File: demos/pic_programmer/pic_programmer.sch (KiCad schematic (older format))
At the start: 50 parts, among them J1 DB9-FEMAL, P1 CONN_2, Q1 BC237, Q2 BC307, Q3 BC307, U2 74HC125, U3 7805, U4 LT1373

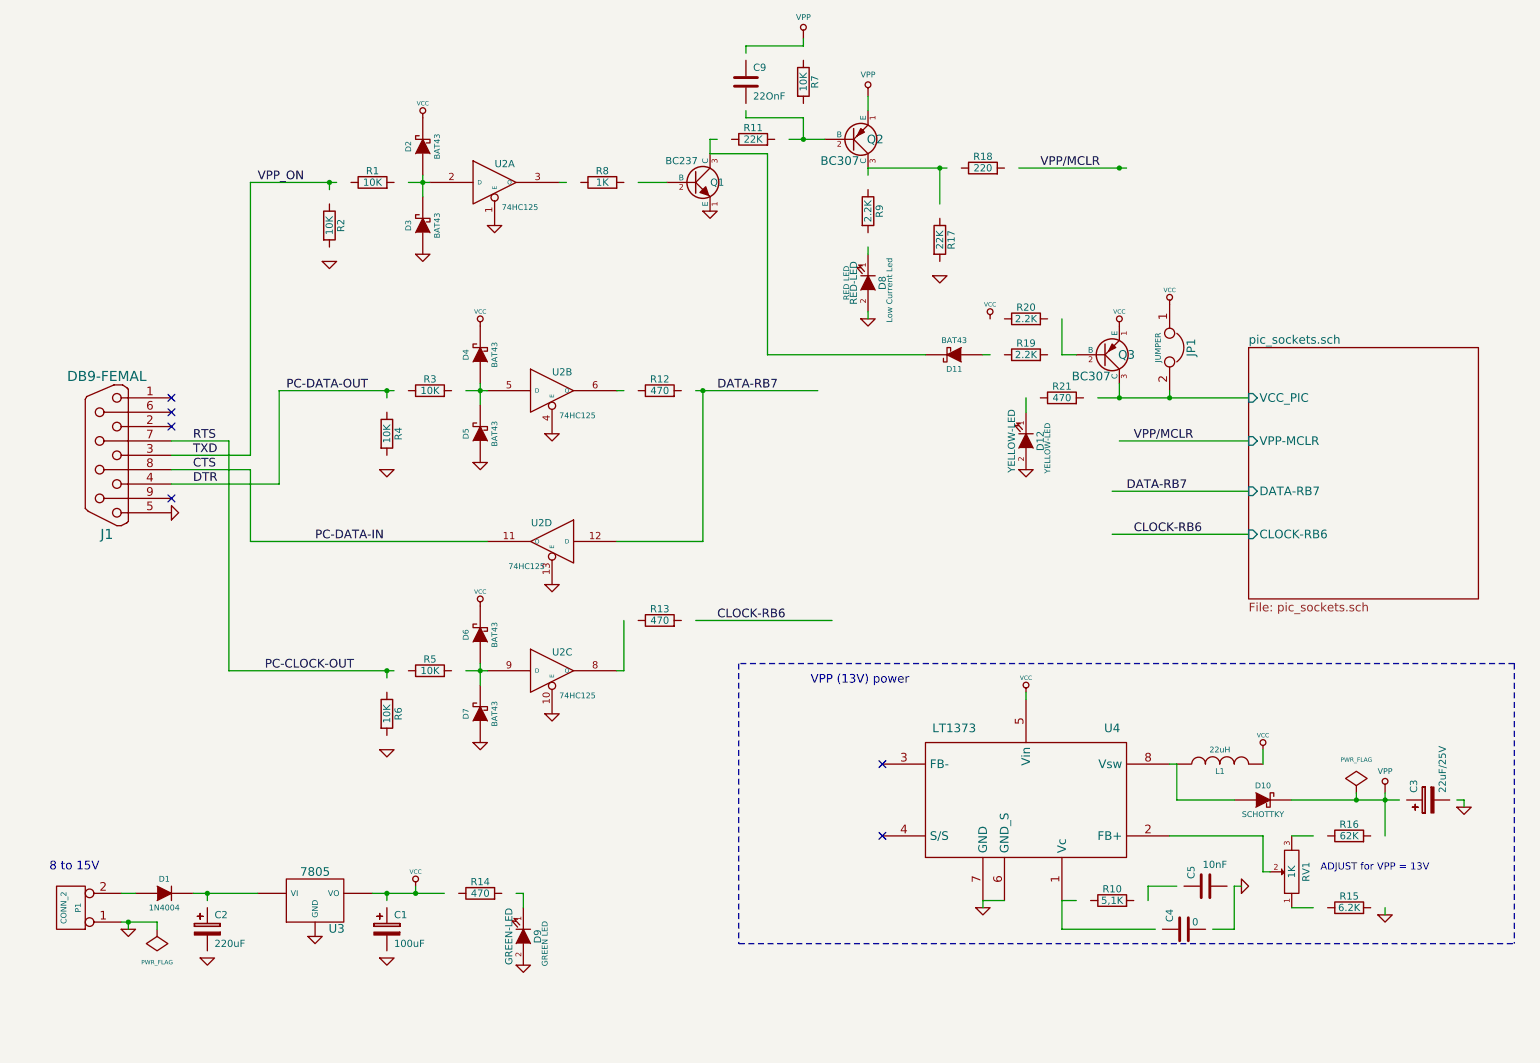
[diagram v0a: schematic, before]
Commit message: Update demos. Fix  pspice netlist issues when using ( and ) in net names ( parenthesis are replaced by underscore) .
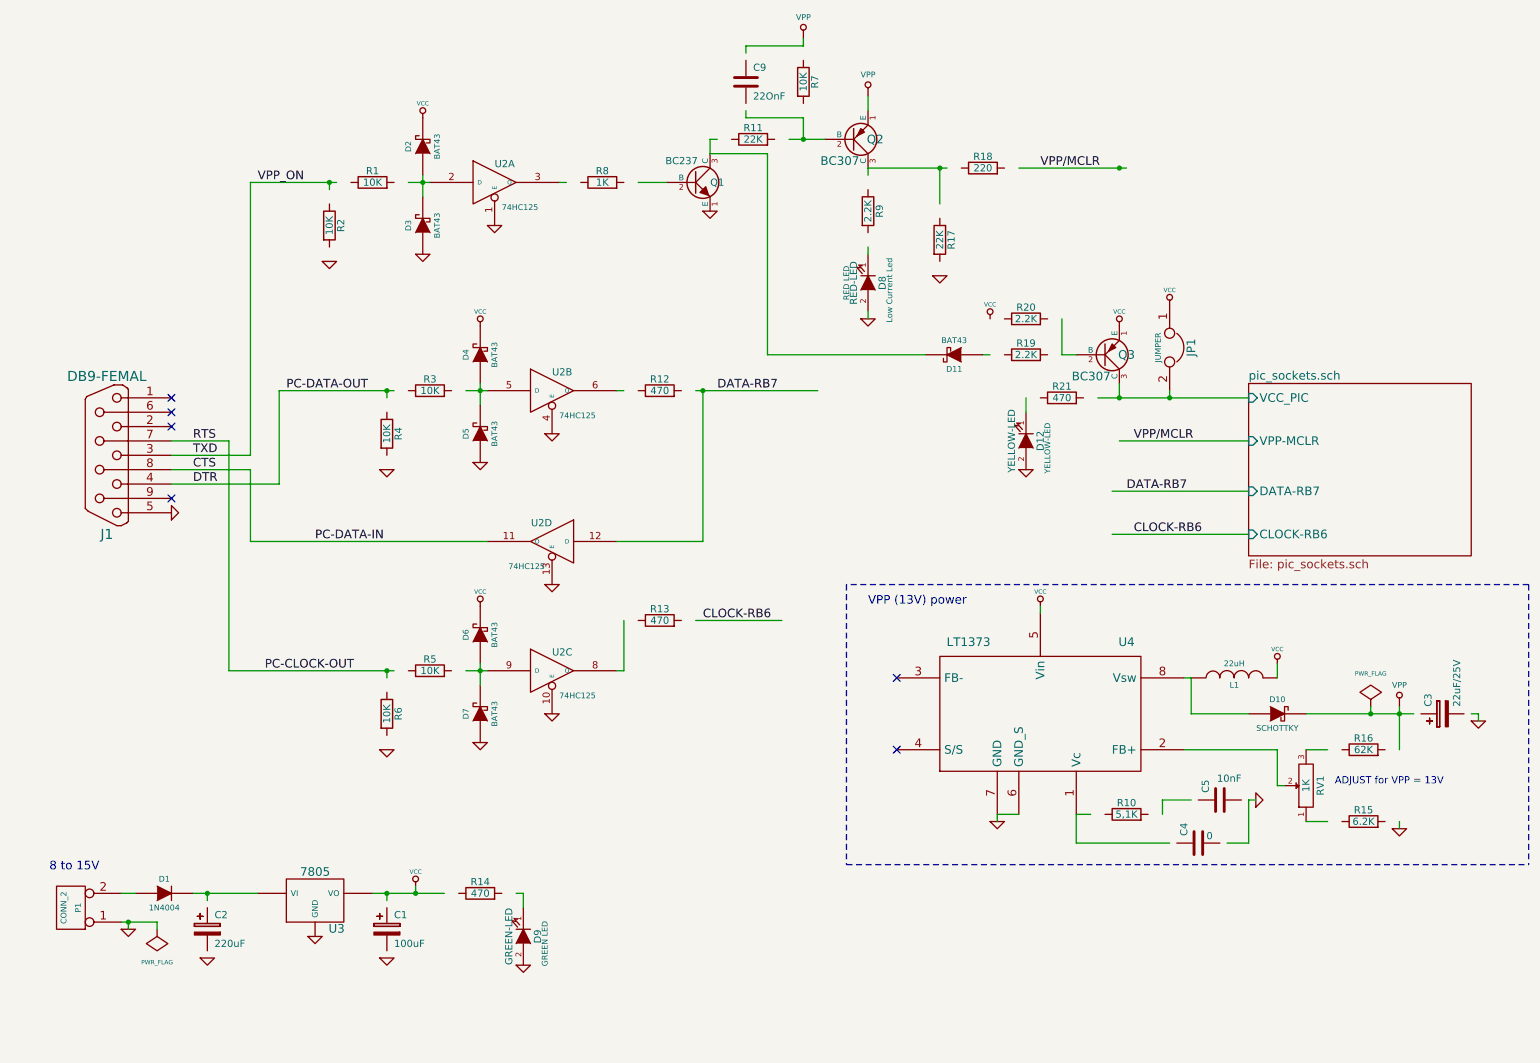
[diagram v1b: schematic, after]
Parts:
- D12: Champ4 (none) -> YELLOW-LED
- D8: Champ4 (none) -> Low Current Led; Champ5 (none) -> RED LED
- D9: Champ4 (none) -> GREEN LED
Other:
- moved on the sheet: C3, C4, C5, D10, L1, R10, R15, R16, RV1, U4

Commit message: Pcbnew: Minor fix in hotkeys. Demos: add an example to use  a local fp-lib-table and local libs, and update schematics and boards.
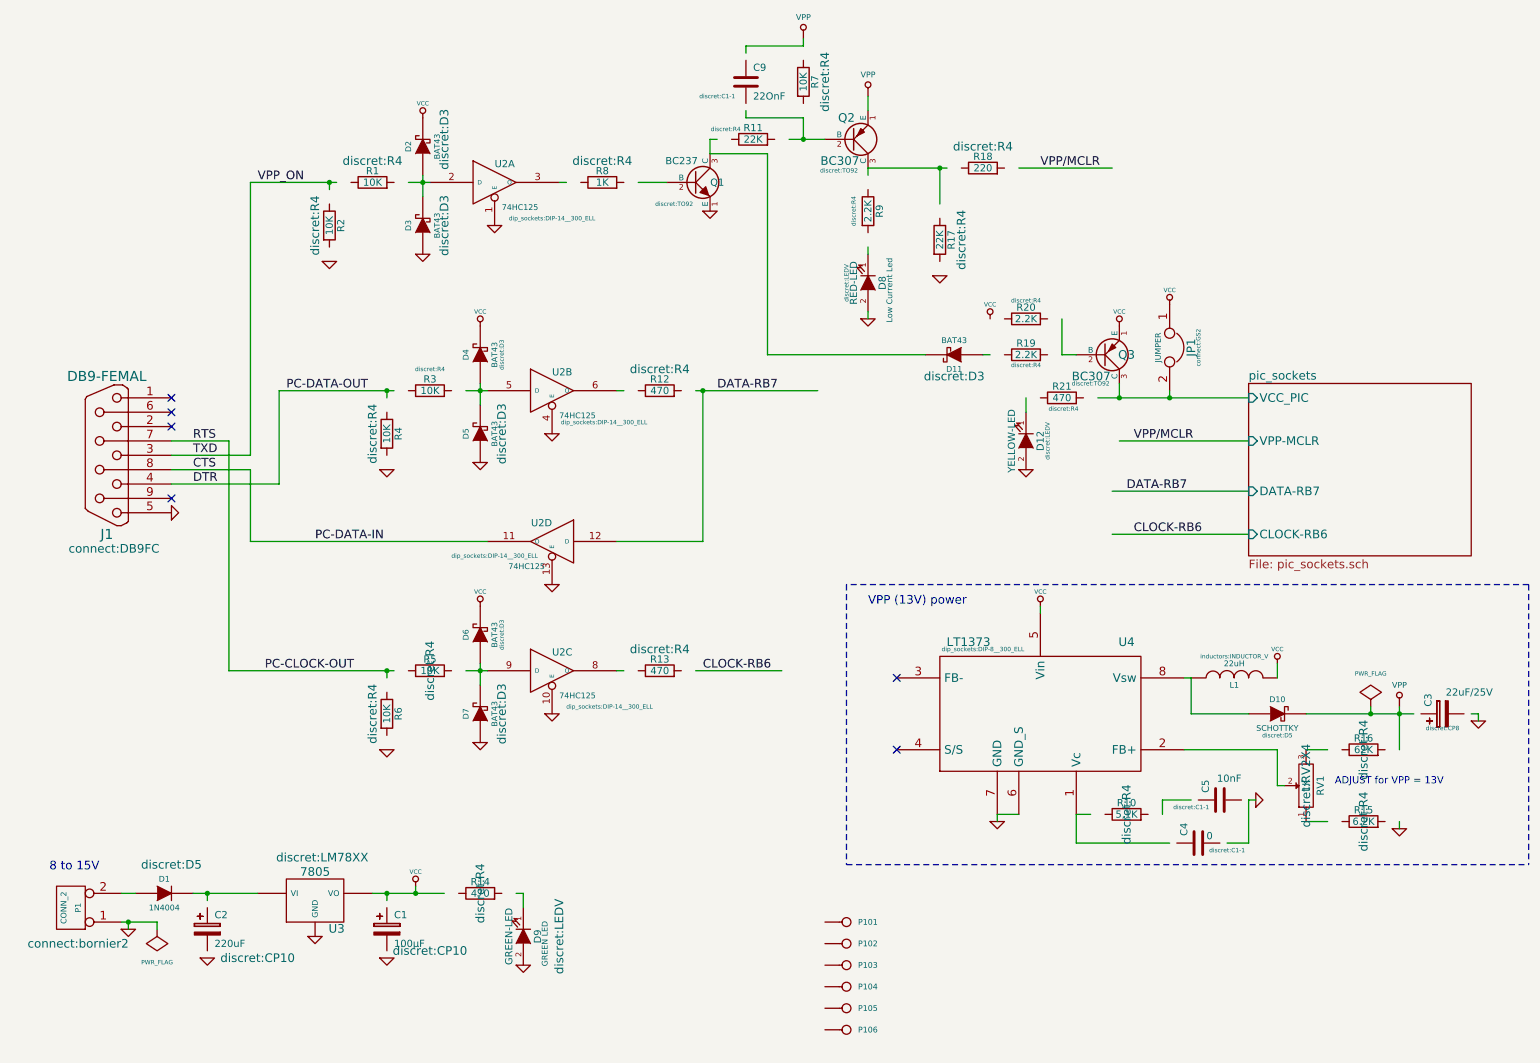
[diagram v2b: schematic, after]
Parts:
- added P101, P102, P103, P104, P105, P106: CONN_1, footprints:1pin-4, symbol CONN_1
- C1: value 100uF -> 100µF; footprint (none) -> discret:CP10
- C2: footprint (none) -> discret:CP10
- C3: footprint (none) -> discret:CP8
- C4, C5, C9: footprint (none) -> discret:C1-1
- D1, D10: footprint (none) -> discret:D5
- D11, D2, D3, D4, D5, D6, D7: footprint (none) -> discret:D3
- D12: footprint (none) -> discret:LEDV; Champ4 YELLOW-LED -> (none)
- D8: footprint (none) -> discret:LEDV; Champ5 RED LED -> (none)
- D9: footprint (none) -> discret:LEDV
- J1: footprint (none) -> connect:DB9FC
- JP1: footprint (none) -> connect:GS2
- L1: footprint (none) -> inductors:INDUCTOR_V
- P1: footprint (none) -> connect:bornier2
- Q1, Q2, Q3: footprint (none) -> discret:TO92
- R1, R10, R11, R12, R13, R14, R15, R16, R17, R18, R19, R2, R20, R21, R3, R4, R5, R6, R7, R8, R9: footprint (none) -> discret:R4
- RV1: footprint (none) -> discret:RV2X4
- U2: footprint (none) -> dip_sockets:DIP-14__300_ELL
- U3: footprint (none) -> discret:LM78XX
- U4: footprint (none) -> dip_sockets:DIP-8__300_ELL
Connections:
- wire segments 96 -> 95
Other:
- moved on the sheet: R13

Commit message: Minor fixes: specctra export: skip malformed circles (having a radius = 0)  in board outline creation, which can crash 3d-viewer or vrml export. dialog_fp_lib_table: remember during a session the last open table (global or local). drawing_tool: fix compil warning Update demos.
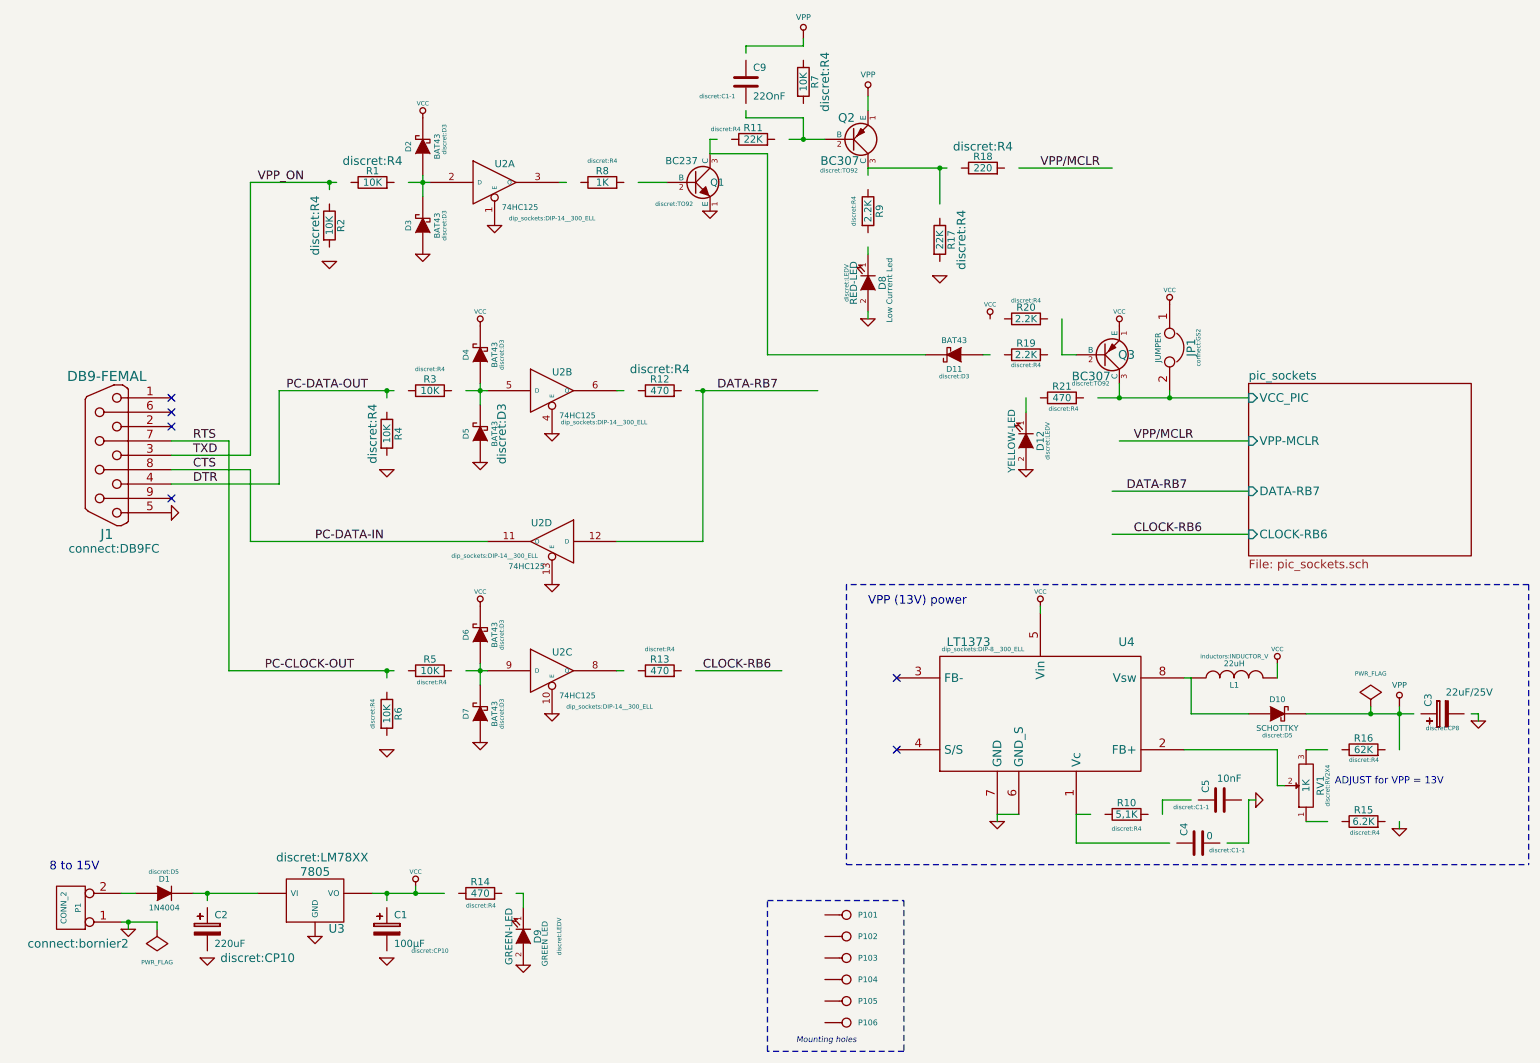
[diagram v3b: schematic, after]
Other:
- note added: "Mounting holes"
- moved on the sheet: P101, P102, P103, P104, P105, P106
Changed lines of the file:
@@
 F 0 "D11" H 7150 3000 40  0000 C CNN
 F 1 "BAT43" H 7150 2800 40  0000 C CNN
-F 2 "discret:D3" H 7150 3050 60  0000 C CNN
+F 2 "discret:D3" H 7150 3050 30  0000 C CNN
 F 3 "" H 7150 2900 60  0001 C CNN
 	1    7150 2900
@@
 F 0 "RV1" H 9600 5800 50  0000 C CNN
 F 1 "1K" H 9600 5900 50  0000 C CNN
-F 2 "discret:RV2X4" H 9600 5900 60  0000 C CNN
+F 2 "discret:RV2X4" H 9600 5750 30  0000 C CNN
 F 3 "" H 9600 5900 60  0001 C CNN
 	1    9600 5900
@@
 F 0 "R10" V 8430 6100 50  0000 C CNN
 F 1 "5,1K" V 8350 6100 50  0000 C CNN
-F 2 "discret:R4" H 8350 6100 60  0000 C CNN
+F 2 "discret:R4" V 8250 6100 30  0000 C CNN
 F 3 "" H 8350 6100 60  0001 C CNN
 	1    8350 6100
@@
 F 0 "R16" V 10080 5650 50  0000 C CNN
 F 1 "62K" V 10000 5650 50  0000 C CNN
-F 2 "discret:R4" H 10000 5650 60  0000 C CNN
+F 2 "discret:R4" V 9929 5647 30  0000 C CNN
 F 3 "" H 10000 5650 60  0001 C CNN
 	1    10000 5650
@@
 F 0 "R15" V 10080 6150 50  0000 C CNN
 F 1 "6.2K" V 10000 6150 50  0000 C CNN
-F 2 "discret:R4" H 10000 6150 60  0000 C CNN
+F 2 "discret:R4" V 9922 6141 30  0000 C CNN
 F 3 "" H 10000 6150 60  0001 C CNN
 	1    10000 6150
@@
 F 0 "D9" H 4150 7050 50  0000 C CNN
 F 1 "GREEN-LED" H 4150 6850 50  0000 C CNN
-F 2 "discret:LEDV" H 4150 7200 60  0000 C CNN
+F 2 "discret:LEDV" H 4150 7200 30  0000 C CNN
 F 3 "" H 4150 6950 60  0001 C CNN
 F 4 "GREEN LED" H 4200 7100 40  0000 C CNN "Champ4"
@@
 F 0 "R14" V 3930 6650 50  0000 C CNN
 F 1 "470" V 3850 6650 50  0000 C CNN
-F 2 "discret:R4" H 3850 6650 60  0000 C CNN
+F 2 "discret:R4" V 3765 6645 30  0000 C CNN
 F 3 "" H 3850 6650 60  0001 C CNN
 	1    3850 6650
@@
 F 0 "C1" H 3250 7000 50  0000 L CNN
 F 1 "100µF" H 3250 6800 50  0000 L CNN
-F 2 "discret:CP10" H 3500 6750 60  0000 C CNN
+F 2 "discret:CP10" H 3500 6750 30  0000 C CNN
 F 3 "" H 3200 6900 60  0001 C CNN
 	1    3200 6900
@@
 F 0 "D1" H 1650 6750 40  0000 C CNN
 F 1 "1N4004" H 1650 6550 40  0000 C CNN
-F 2 "discret:D5" H 1700 6850 60  0000 C CNN
+F 2 "discret:D5" H 1646 6800 30  0000 C CNN
 F 3 "" H 1650 6650 60  0001 C CNN
 	1    1650 6650
@@
 F 0 "R8" V 4780 1700 50  0000 C CNN
 F 1 "1K" V 4700 1700 50  0000 C CNN
-F 2 "discret:R4" V 4850 1700 60  0000 C CNN
+F 2 "discret:R4" V 4850 1700 30  0000 C CNN
 F 3 "" H 4700 1700 60  0001 C CNN
 	1    4700 1700
@@
 F 0 "R13" V 5180 5100 50  0000 C CNN
 F 1 "470" V 5100 5100 50  0000 C CNN
-F 2 "discret:R4" V 5250 5100 60  0000 C CNN
+F 2 "discret:R4" V 5250 5100 30  0000 C CNN
 F 3 "" H 5100 5100 60  0001 C CNN
 	1    5100 5100
@@
 F 0 "D7" H 3850 5500 40  0000 C CNN
 F 1 "BAT43" H 3850 5300 40  0000 C CNN
-F 2 "discret:D3" H 3850 5250 60  0000 C CNN
+F 2 "discret:D3" H 3850 5250 30  0000 C CNN
 F 3 "" H 3850 5400 60  0001 C CNN
 	1    3850 5400
@@
 F 0 "R6" V 3280 5400 50  0000 C CNN
 F 1 "10K" V 3200 5400 50  0000 C CNN
-F 2 "discret:R4" V 3100 5400 60  0000 C CNN
+F 2 "discret:R4" V 3100 5400 30  0000 C CNN
 F 3 "" H 3200 5400 60  0001 C CNN
 	1    3200 5400
@@
 F 0 "R5" V 3580 5100 50  0000 C CNN
 F 1 "10K" V 3500 5100 50  0000 C CNN
-F 2 "discret:R4" H 3500 5100 60  0000 C CNN
+F 2 "discret:R4" V 3420 5088 30  0000 C CNN
 F 3 "" H 3500 5100 60  0001 C CNN
 	1    3500 5100
@@
 F 0 "D3" H 3450 2100 40  0000 C CNN
 F 1 "BAT43" H 3450 1900 40  0000 C CNN
-F 2 "discret:D3" H 3450 1850 60  0000 C CNN
+F 2 "discret:D3" H 3450 1850 30  0000 C CNN
 F 3 "" H 3450 2000 60  0001 C CNN
 	1    3450 2000
@@
 F 0 "D2" H 3450 1550 40  0000 C CNN
 F 1 "BAT43" H 3450 1350 40  0000 C CNN
-F 2 "discret:D3" H 3500 1300 60  0000 C CNN
+F 2 "discret:D3" H 3500 1300 30  0000 C CNN
 F 3 "" H 3450 1450 60  0001 C CNN
 	1    3450 1450
@@
 L CONN_1 P101
 U 1 1 54020BEA
-P 6400 6850
-F 0 "P101" H 6480 6850 40  0000 L CNN
-F 1 "CONN_1" H 6400 6905 30  0001 C CNN
-F 2 "footprints:1pin-4" H 6400 6850 60  0001 C CNN
-F 3 "" H 6400 6850 60  0000 C CNN
-	1    6400 6850
+P 6400 6800
+F 0 "P101" H 6480 6800 40  0000 L CNN
+F 1 "CONN_1" H 6400 6855 30  0001 C CNN
+F 2 "footprints:1pin-4" H 6400 6800 60  0001 C CNN
+F 3 "" H 6400 6800 60  0000 C CNN
+	1    6400 6800
 	1    0    0    -1
 $EndComp
@@
 L CONN_1 P102
 U 1 1 54020DA9
-P 6400 7000
-F 0 "P102" H 6480 7000 40  0000 L CNN
-F 1 "CONN_1" H 6400 7055 30  0001 C CNN
-F 2 "footprints:1pin-4" H 6400 7000 60  0001 C CNN
-F 3 "" H 6400 7000 60  0000 C CNN
-	1    6400 7000
+P 6400 6950
+F 0 "P102" H 6480 6950 40  0000 L CNN
+F 1 "CONN_1" H 6400 7005 30  0001 C CNN
+F 2 "footprints:1pin-4" H 6400 6950 60  0001 C CNN
+F 3 "" H 6400 6950 60  0000 C CNN
+	1    6400 6950
 	1    0    0    -1
 $EndComp
@@
 L CONN_1 P103
 U 1 1 54020DC2
-P 6400 7150
-F 0 "P103" H 6480 7150 40  0000 L CNN
-F 1 "CONN_1" H 6400 7205 30  0001 C CNN
-F 2 "footprints:1pin-4" H 6400 7150 60  0001 C CNN
-F 3 "" H 6400 7150 60  0000 C CNN
-	1    6400 7150
+P 6400 7100
+F 0 "P103" H 6480 7100 40  0000 L CNN
+F 1 "CONN_1" H 6400 7155 30  0001 C CNN
+F 2 "footprints:1pin-4" H 6400 7100 60  0001 C CNN
+F 3 "" H 6400 7100 60  0000 C CNN
+	1    6400 7100
 	1    0    0    -1
 $EndComp
@@
 L CONN_1 P104
 U 1 1 54020DE3
-P 6400 7300
-F 0 "P104" H 6480 7300 40  0000 L CNN
-F 1 "CONN_1" H 6400 7355 30  0001 C CNN
-F 2 "footprints:1pin-4" H 6400 7300 60  0001 C CNN
-F 3 "" H 6400 7300 60  0000 C CNN
-	1    6400 7300
+P 6400 7250
+F 0 "P104" H 6480 7250 40  0000 L CNN
+F 1 "CONN_1" H 6400 7305 30  0001 C CNN
+F 2 "footprints:1pin-4" H 6400 7250 60  0001 C CNN
+F 3 "" H 6400 7250 60  0000 C CNN
+	1    6400 7250
 	1    0    0    -1
 $EndComp
@@
 L CONN_1 P105
 U 1 1 54020E5D
-P 6400 7450
-F 0 "P105" H 6480 7450 40  0000 L CNN
-F 1 "CONN_1" H 6400 7505 30  0001 C CNN
-F 2 "footprints:1pin-4" H 6400 7450 60  0001 C CNN
-F 3 "" H 6400 7450 60  0000 C CNN
-	1    6400 7450
+P 6400 7400
+F 0 "P105" H 6480 7400 40  0000 L CNN
+F 1 "CONN_1" H 6400 7455 30  0001 C CNN
+F 2 "footprints:1pin-4" H 6400 7400 60  0001 C CNN
+F 3 "" H 6400 7400 60  0000 C CNN
+	1    6400 7400
 	1    0    0    -1
 $EndComp
@@
 L CONN_1 P106
 U 1 1 54020E76
-P 6400 7600
-F 0 "P106" H 6480 7600 40  0000 L CNN
-F 1 "CONN_1" H 6400 7655 30  0001 C CNN
-F 2 "footprints:1pin-4" H 6400 7600 60  0001 C CNN
-F 3 "" H 6400 7600 60  0000 C CNN
-	1    6400 7600
+P 6400 7550
+F 0 "P106" H 6480 7550 40  0000 L CNN
+F 1 "CONN_1" H 6400 7605 30  0001 C CNN
+F 2 "footprints:1pin-4" H 6400 7550 60  0001 C CNN
+F 3 "" H 6400 7550 60  0000 C CNN
+	1    6400 7550
 	1    0    0    -1
 $EndComp
 Connection ~ 8650 3200
+Wire Notes Line
+	5850 6700 6800 6700
+Wire Notes Line
+	6800 6700 6800 7750
+Wire Notes Line
+	6800 7750 5850 7750
+Wire Notes Line
+	5850 7750 5850 6700
+Text Notes 6050 7700 0    40   Italic 0
+Mounting holes
 $EndSCHEMATC
